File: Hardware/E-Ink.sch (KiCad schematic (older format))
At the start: 0 parts

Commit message: Martin ist unförmig
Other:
- note added: "Battery Monitoring"
- note added: "Inputs and Outputs"
- note added: "Microcontroller"
- note added: "Power"

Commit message: save work at arges, finished layout and routing
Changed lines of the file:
@@
 EESchema Schematic File Version 4
 LIBS:E-Ink-cache
-EELAYER 29 0
+EELAYER 30 0
 EELAYER END
 $Descr A4 11693 8268
@@
 	4350 3050 4400 3050
 Text GLabel 4400 3150 2    50   Input ~ 0
-GPIO_VMess
+GPIO_Vmess
 Wire Wire Line
 	4400 3150 4350 3150
@@
 Text GLabel 2900 2800 0    50   Output ~ 0
 MOSI
+Text GLabel 2900 3000 0    50   Output ~ 0
+SCK
 Text GLabel 2900 2900 0    50   Output ~ 0
-SCK
-Text GLabel 2900 3000 0    50   Output ~ 0
 CS
 Text GLabel 2850 5400 0    50   Input ~ 0

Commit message: Save work at Arges
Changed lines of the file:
@@
 EESchema Schematic File Version 4
+LIBS:E-Ink-cache
 EELAYER 30 0
 EELAYER END
@@
 Text GLabel 2850 5500 0    50   Output ~ 0
 MOSI
+Text GLabel 2850 5700 0    50   Output ~ 0
+SCK
 Text GLabel 2850 5600 0    50   Output ~ 0
-SCK
-Text GLabel 2850 5700 0    50   Output ~ 0
 CS
 Wire Wire Line

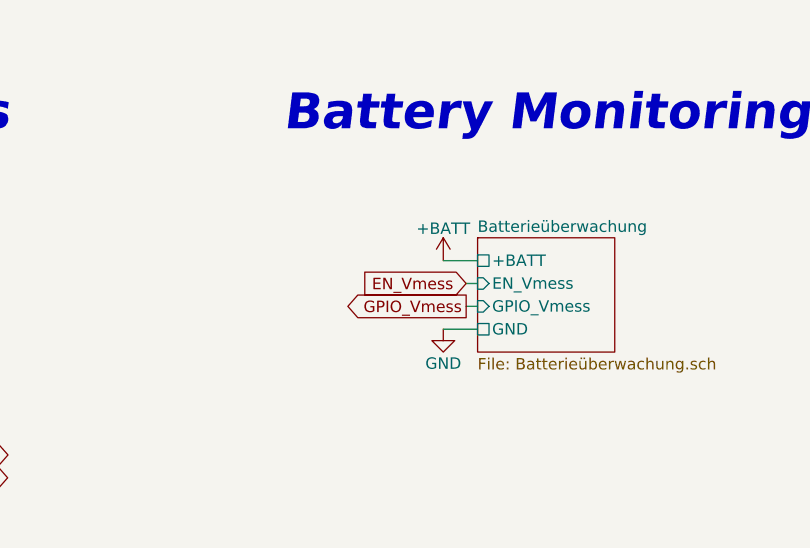
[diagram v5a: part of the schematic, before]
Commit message: Added new MCU and redesigned schematics
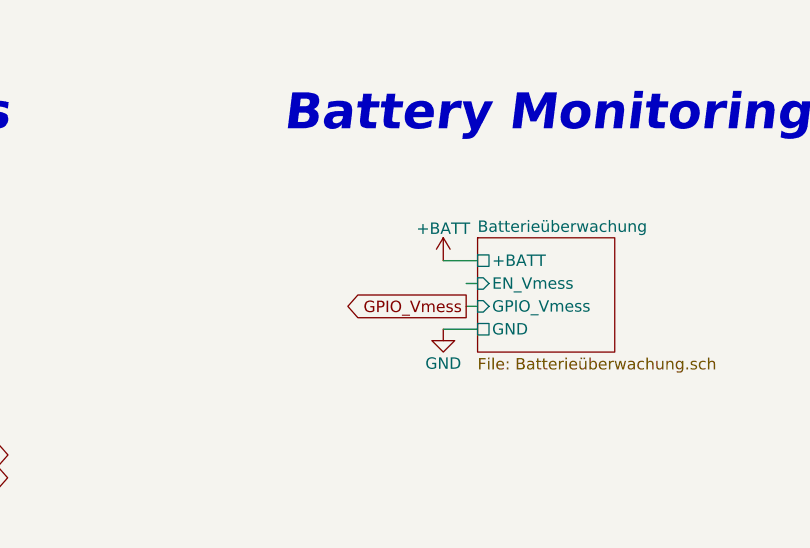
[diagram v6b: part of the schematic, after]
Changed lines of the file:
@@
 EESchema Schematic File Version 4
-LIBS:E-Ink-cache
 EELAYER 30 0
 EELAYER END
@@
 Wire Wire Line
 	6750 5000 6900 5000
-Text GLabel 6850 5100 0    50   Input ~ 0
-EN_Vmess
 Wire Wire Line
 	6850 5100 6900 5100

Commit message: finished PCB, Thursday Review with Lukas
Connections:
- net labels removed: EN_Vmess
- wire segments 41 -> 40
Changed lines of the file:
@@
 F0 "Batterieüberwachung" 50
 F1 "Batterieüberwachung.sch" 50
-F2 "EN_Vmess" I L 6900 5100 50
-F3 "+BATT" U L 6900 5000 50
-F4 "GPIO_Vmess" I L 6900 5200 50
-F5 "GND" U L 6900 5300 50
+F2 "+BATT" U L 6900 5000 50
+F3 "GPIO_Vmess" I L 6900 5200 50
+F4 "GND" U L 6900 5300 50
 $EndSheet
 $Comp
@@
 F8 "RXD0" I R 4350 2450 50
 F9 "EN_5V" O R 4350 2950 50
-F10 "EN_Vmess" O R 4350 3050 50
-F11 "CS" O L 2950 2900 50
-F12 "SCK" O L 2950 3000 50
-F13 "MOSI" O L 2950 2800 50
-F14 "PROG_ESP" I R 4350 3350 50
-F15 "RST_DIS" O R 4350 2650 50
-F16 "BSY_DIS" I R 4350 2750 50
+F10 "CS" O L 2950 2900 50
+F11 "SCK" O L 2950 3000 50
+F12 "MOSI" O L 2950 2800 50
+F13 "PROG_ESP" I R 4350 3350 50
+F14 "RST_DIS" O R 4350 2650 50
+F15 "BSY_DIS" I R 4350 2750 50
 $EndSheet
 $Comp
@@
 F0 "IO-Platine" 50
 F1 "IO-Platine.sch" 50
-F2 "EN_SPI" I L 2950 5300 50
-F3 "CS" I L 2950 5600 50
-F4 "SCK" I L 2950 5700 50
-F5 "MOSI" I L 2950 5500 50
-F6 "MISO" O L 2950 5400 50
-F7 "RST_ESP" O R 4350 5950 50
-F8 "+3V3" U L 2950 4900 50
-F9 "+5V" U L 2950 5000 50
-F10 "GND" U L 2950 5950 50
-F11 "RST_DIS" I R 4350 5400 50
-F12 "BSY_DIS" O R 4350 5500 50
-F13 "PROG_ESP" O R 4350 5850 50
-F14 "+BATT" U L 2950 5100 50
-F15 "RX_D0" O R 4350 5000 50
-F16 "TX_D0" I R 4350 4900 50
+F2 "CS" I L 2950 5600 50
+F3 "SCK" I L 2950 5700 50
+F4 "MOSI" I L 2950 5500 50
+F5 "MISO" O L 2950 5400 50
+F6 "RST_ESP" O R 4350 5950 50
+F7 "+3V3" U L 2950 4900 50
+F8 "+5V" U L 2950 5000 50
+F9 "GND" U L 2950 5950 50
+F10 "RST_DIS" I R 4350 5400 50
+F11 "BSY_DIS" O R 4350 5500 50
+F12 "PROG_ESP" O R 4350 5850 50
+F13 "+BATT" U L 2950 5100 50
+F14 "RX_D0" O R 4350 5000 50
+F15 "TX_D0" I R 4350 4900 50
 $EndSheet
 $Comp
@@
 Text GLabel 4400 2950 2    50   Output ~ 0
 EN_5V
-Text GLabel 4400 3050 2    50   Output ~ 0
-EN_Vmess
 Wire Wire Line
 	4400 2950 4350 2950
@@
 Wire Wire Line
 	4350 3450 4400 3450
-Text GLabel 2850 5300 0    50   Input ~ 0
-EN_5V
-Wire Wire Line
-	2850 5300 2950 5300
 $Comp
 L power:GND #PWR0104
